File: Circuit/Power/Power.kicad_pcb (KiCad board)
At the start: 2 copper layers, 78.7 x 45.7 mm, 25 parts, among them J1 +-12V Pulse in, J2 To Starter & Coil, J3 To Capacitors, J4 From Control, J5 12V DC in, Q1 IRFP250NPBF, Q2 IRFP250NPBF, Q3 IRFP250NPBF, Q4 IRFP250NPBF, Q5 IRFP250NPBF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

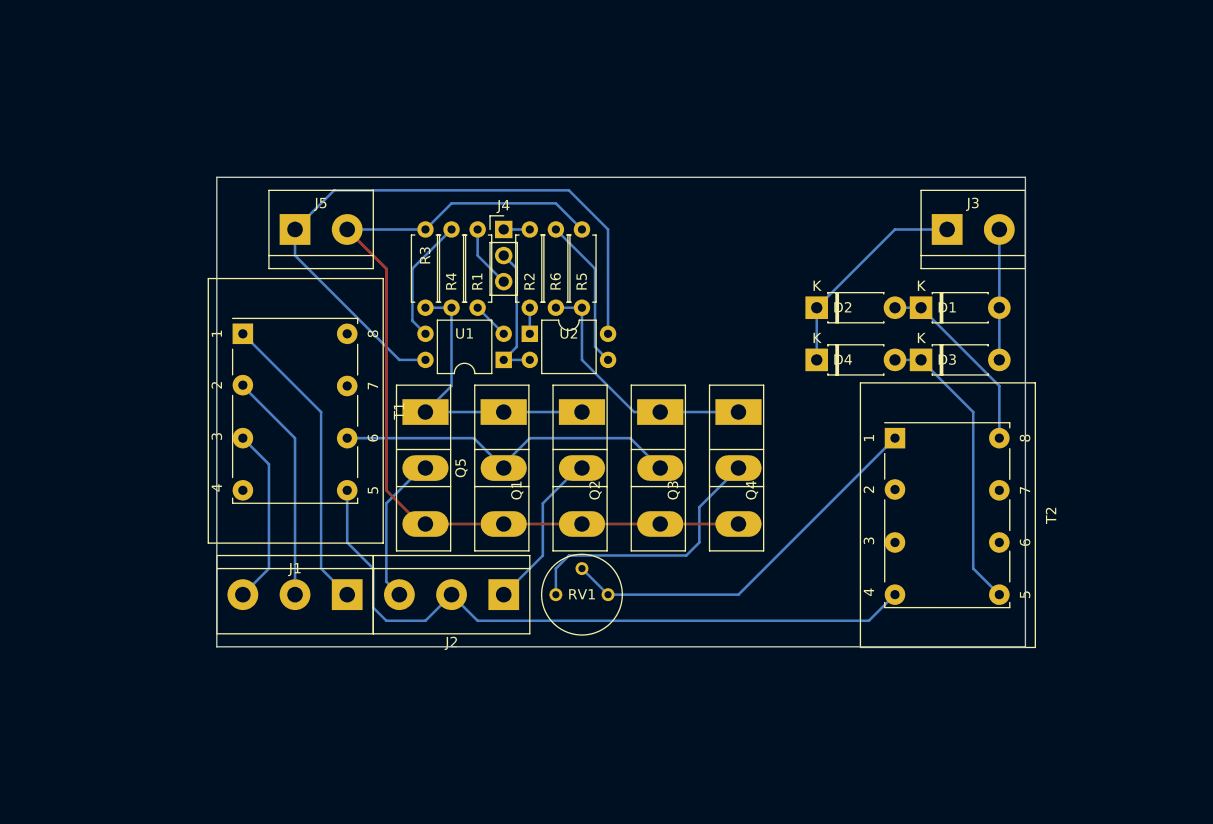
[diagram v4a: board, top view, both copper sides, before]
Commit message: [Circuit] Add a 1-stage Cockcroft–Walton generator to power module
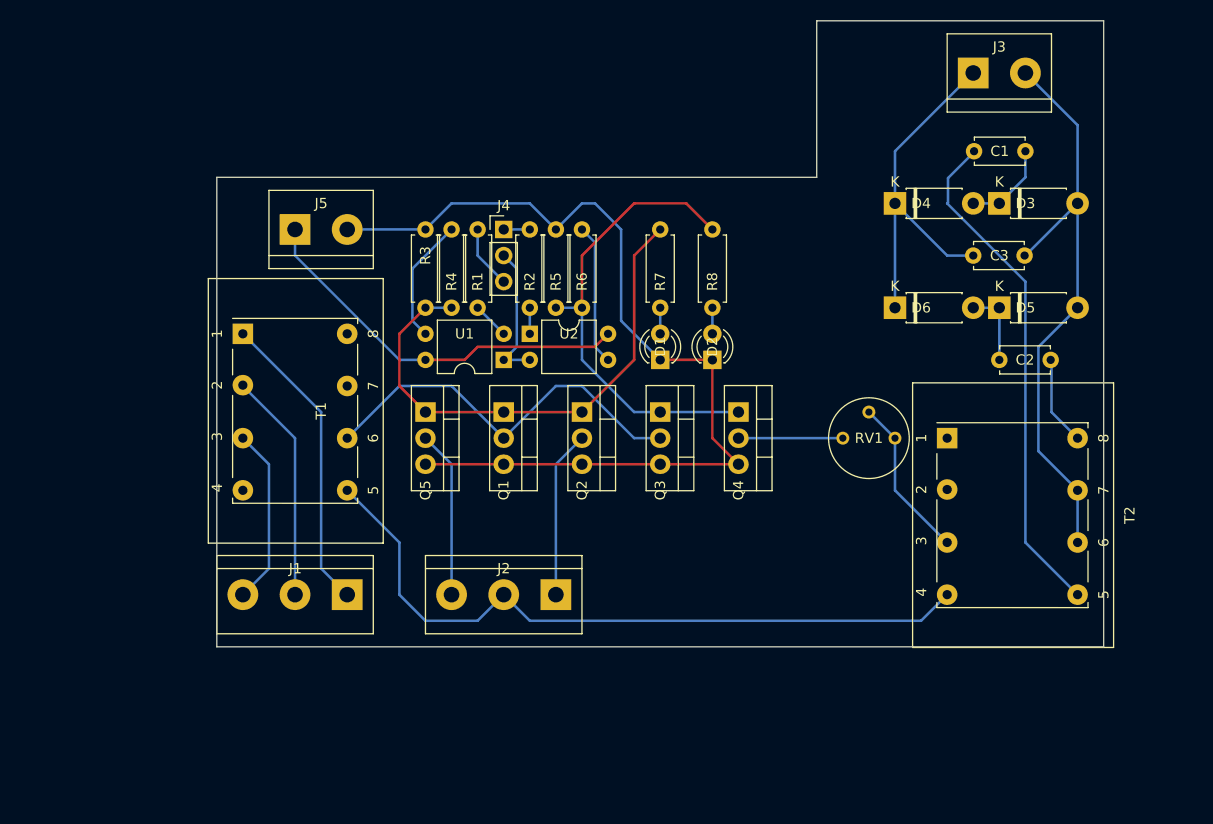
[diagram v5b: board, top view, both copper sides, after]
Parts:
- added C1: 1nF, Capacitor_THT:C_Disc_D4.7mm_W2.5mm_P5.00mm, F.Cu at (147.3, 33.0)
- added C2: 1nF, Capacitor_THT:C_Disc_D4.7mm_W2.5mm_P5.00mm, F.Cu at (144.8, 53.3)
- added C3: 1nF, Capacitor_THT:C_Disc_D4.7mm_W2.5mm_P5.00mm, F.Cu at (142.2, 43.2)
- added D1: LED, LED_THT:LED_D3.0mm_FlatTop, F.Cu at (111.8, 53.3)
- added D2: LED, LED_THT:LED_D3.0mm_FlatTop, F.Cu at (116.8, 53.3)
- added R7: 2K2, Resistor_THT:R_Axial_DIN0207_L6.3mm_D2.5mm_P7.62mm_Horizontal, F.Cu at (111.8, 48.3)
- added R8: 2K2, Resistor_THT:R_Axial_DIN0207_L6.3mm_D2.5mm_P7.62mm_Horizontal, F.Cu at (116.8, 40.6)
- J1: value +-12V Pulse in -> 12V AC in
- Q1, Q2, Q3, Q4, Q5: value IRFP250NPBF -> RFP30N06LE; footprint Package_TO_SOT_THT:TO-247-3_Vertical -> Package_TO_SOT_THT:TO-220-3_Vertical
- R4, R6: value 100 -> 10K
- T1: value 4+4:8 -> 3+3:6
- moved RV1 31.8 mm to (129.5, 61.0)
- moved J3 15.5 mm to (142.2, 25.4)
- moved D3 12.7 mm to (144.8, 38.1)
- moved D4 12.7 mm to (134.6, 38.1)
- moved D5 9.16 mm to (144.8, 48.3)
- moved D6 9.16 mm to (134.6, 48.3)
- moved J2 5.08 mm to (101.6, 76.2)
- moved T2 5.08 mm to (139.7, 61.0)
- moved R5 2.54 mm to (101.6, 48.3)
- moved R6 2.54 mm to (104.1, 40.6)
- renumbered D1 to D3, D2 to D4, D3 to D5, D4 to D6
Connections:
- net /+12VPulseIn renamed /AC+In
- net /-12VPulseIn renamed /AC-In
- net /0Vin renamed /AC0In
- D3 pad 1: Net-(D1-Pad1) -> Net-(C1-Pad1)
- D4 pad 2: Net-(D1-Pad1) -> Net-(C1-Pad1)
- D5 pad 1: Net-(D3-Pad1) -> Net-(C2-Pad1)
- D6 pad 2: Net-(D3-Pad1) -> Net-(C2-Pad1)
- T2 pad 1: Net-(RV1-Pad2) -> (no net)
- T2 pad 3: (no net) -> Net-(RV1-Pad2)
- T2 pad 5: Net-(D3-Pad1) -> Net-(C1-Pad2)
- T2 pad 6: (no net) -> /CapacitorPower-
- T2 pad 7: (no net) -> /CapacitorPower-
- T2 pad 8: Net-(D1-Pad1) -> Net-(C2-Pad2)
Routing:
- net Net-(C1-Pad2): track 0.00 -> 49.5 mm
- net /CapacitorPower-: track 12.7 -> 58.2 mm
- net Net-(D3-Pad1): track 28.6 -> 0.00 mm
- net +12V: track 63.2 -> 38.3 mm
- net Net-(Q1-Pad1): track 29.0 -> 51.0 mm
- net Net-(RV1-Pad2): track 37.8 -> 15.9 mm
- net Net-(Q3-Pad1): track 25.0 -> 45.9 mm
- net Net-(D1-Pad1): track 18.4 -> 0.00 mm
- net Net-(Q4-Pad2): track 26.4 -> 10.2 mm
- net /CapacitorPower+: track 20.9 -> 35.7 mm
- net Net-(C2-Pad2): track 0.00 -> 8.67 mm
- net Net-(C1-Pad1): track 0.00 -> 8.67 mm
- net Net-(C2-Pad1): track 0.00 -> 7.62 mm
- net GND: track 87.6 -> 93.0 mm
- net Net-(Q1-Pad2): track 34.3 -> 38.9 mm
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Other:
- board size 78.7 x 45.7 mm -> 86.4 x 61 mm

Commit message: [Circuit] Change the isolation transformer to a toroid one
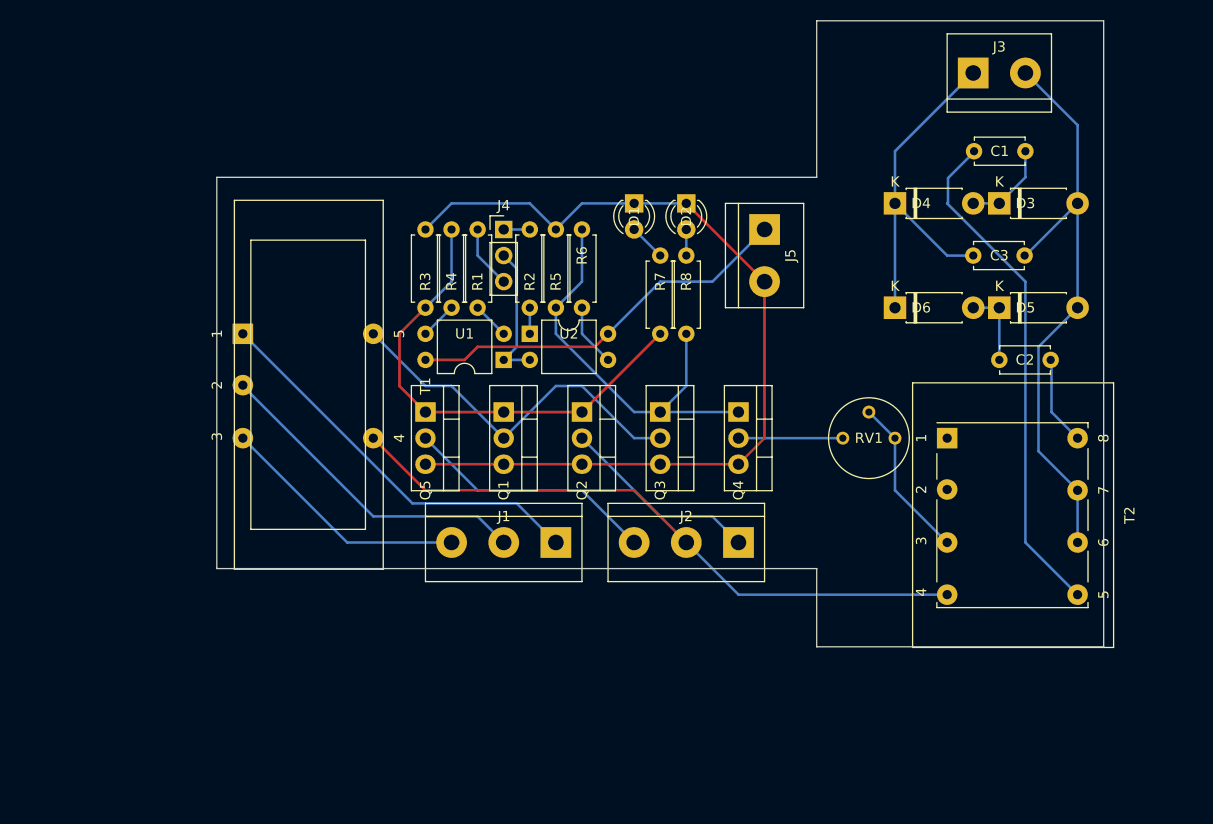
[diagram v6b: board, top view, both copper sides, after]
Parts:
- T1: footprint Power:Transformer_Generic_EE25_8Pin -> Power:Transformer_Toroid_5Pin
- moved J5 45.7 mm to (121.9, 40.6), turned to 270 degrees
- moved J1 20.9 mm to (101.6, 71.1)
- moved J2 18.5 mm to (119.4, 71.1)
- moved D1 15.5 mm to (109.2, 38.1), turned to 270 degrees
- moved D2 15.5 mm to (114.3, 38.1), turned to 270 degrees
- moved R8 10.5 mm to (114.3, 50.8), turned to 90 degrees
- moved R4 7.62 mm to (91.4, 48.3), turned to 90 degrees
- moved R6 7.62 mm to (104.1, 48.3), turned to 90 degrees
- moved T1 7.62 mm to (71.1, 43.2)
- moved R7 5.08 mm to (111.8, 43.2), turned to 270 degrees
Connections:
- T1 pad 4: (no net) -> /StarterPower-
- T1 pad 5: /StarterPower- -> Net-(Q1-Pad2)
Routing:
- net /AC0In: track 22.4 -> 31.8 mm
- net /AC+In: track 29.6 -> 38.9 mm
- net Net-(R4-Pad1): track 12.3 -> 3.59 mm
- net /CoilControl: track 16.3 -> 24.5 mm
- net Net-(R6-Pad1): track 13.8 -> 6.13 mm
- net /StarterPower-: track 69.8 -> 62.2 mm
- net /AC-In: track 17.4 -> 24.6 mm
- net Net-(Q3-Pad1): track 45.9 -> 40.8 mm
- net Net-(Q1-Pad1): track 51.0 -> 47.0 mm
- net GND: track 93.0 -> 89.8 mm
- net /StarterPower+: track 16.3 -> 19.4 mm
- net Net-(Q1-Pad2): track 38.9 -> 36.4 mm
- net Net-(D1-Pad2): track 2.54 -> 3.59 mm
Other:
- outline, holes or cut-outs redrawn

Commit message: [Circuit] Optimize the PCB of power module
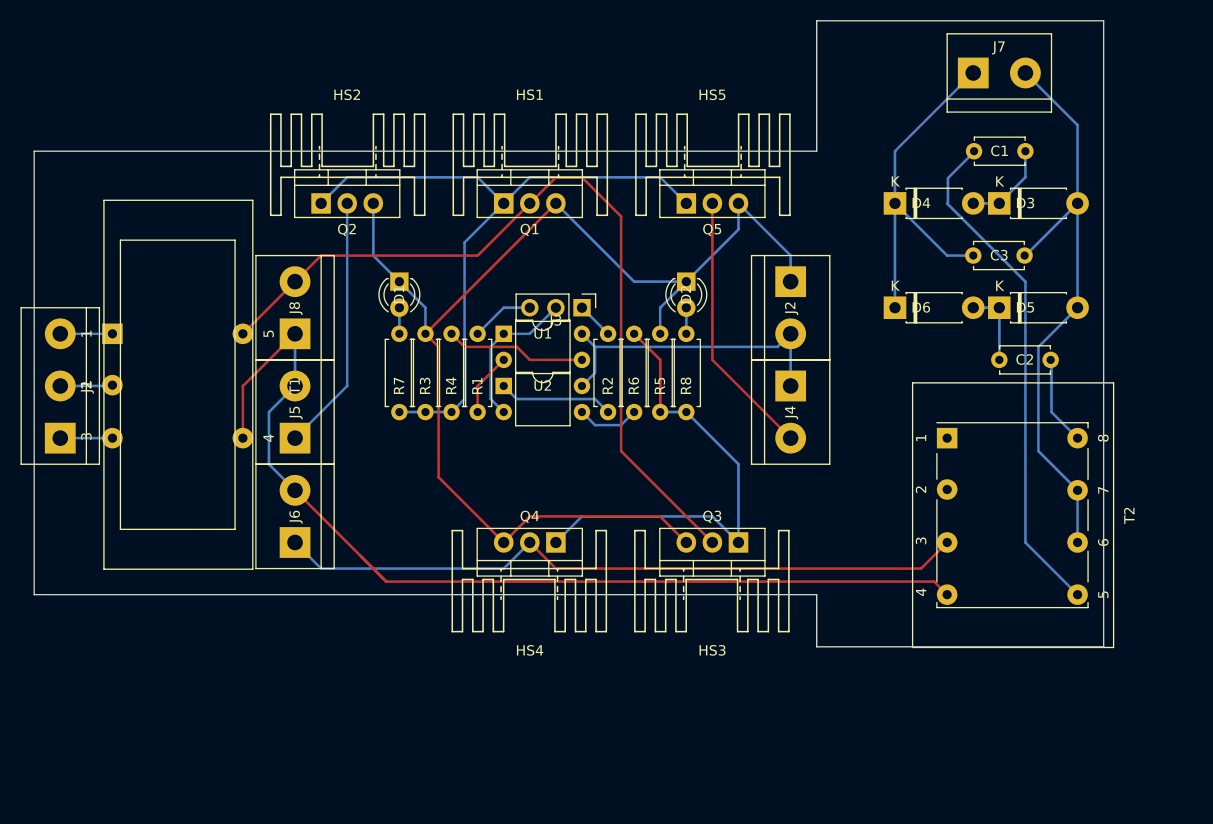
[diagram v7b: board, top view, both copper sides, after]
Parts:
- removed the J2 at (119.4, 71.1)
- removed RV1: 50K, Potentiometer_THT:Potentiometer_Bourns_3339P_Vertical
- added HS1: Heatsink, Power:Heatsink_TO220_15x10mm, F.Cu at (99.1, 35.6)
- added HS2: Heatsink, Power:Heatsink_TO220_15x10mm, F.Cu at (81.3, 35.6)
- added HS3: Heatsink, Power:Heatsink_TO220_15x10mm, F.Cu at (116.8, 73.7)
- added HS4: Heatsink, Power:Heatsink_TO220_15x10mm, F.Cu at (99.1, 73.7)
- added HS5: Heatsink, Power:Heatsink_TO220_15x10mm, F.Cu at (116.8, 35.6)
- added J4: To Coil, TerminalBlock:TerminalBlock_bornier-2_P5.08mm, F.Cu at (124.5, 55.9)
- added J5: To Starter, TerminalBlock:TerminalBlock_bornier-2_P5.08mm, F.Cu at (76.2, 61.0)
- added J6: To Capacitor, TerminalBlock:TerminalBlock_bornier-2_P5.08mm, F.Cu at (76.2, 71.1)
- added J8: AC In, TerminalBlock:TerminalBlock_bornier-2_P5.08mm, F.Cu at (76.2, 50.8)
- D1: value LED -> Discharge
- D2: value LED -> Charge
- J1: value 12V AC in -> 12V AC In
- J2: renamed from J5; value 12V DC in -> DC In
- R7, R8: value 2K2 -> 3K3
- T1: value 3+3:6 -> 7+7:14
- moved J1 49.3 mm to (53.3, 61.0), turned to 90 degrees
- moved Q2 32.5 mm to (78.7, 38.1), turned to 0 degrees
- moved Q5 32.5 mm to (114.3, 38.1), turned to 0 degrees
- moved R7 26.5 mm to (86.4, 50.8)
- moved D1 24.1 mm to (86.4, 45.7)
- moved Q4 21.8 mm to (101.6, 71.1), turned to 180 degrees
- moved Q1 20.3 mm to (96.5, 38.1), turned to 0 degrees
- moved Q3 14.8 mm to (119.4, 71.1), turned to 180 degrees
- moved R5 14.4 mm to (111.8, 58.4)
- moved T1 12.7 mm to (58.4, 43.2)
- moved R2 12.7 mm to (106.7, 50.8)
- moved R6 11.4 mm to (109.2, 58.4)
- moved J3 10.8 mm to (104.1, 48.3), turned to 270 degrees
- moved R1 10.2 mm to (94.0, 50.8)
- moved R3 10.2 mm to (88.9, 50.8)
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- renumbered J4 to J3, J3 to J7
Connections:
- J1 pad 1: /AC+In -> /AC-In
- J1 pad 3: /AC-In -> /AC+In
- J2 pad 1: +12V -> GND
- J2 pad 2: GND -> +12V
- Q4 pad 2: Net-(Q4-Pad2) -> Net-(J6-Pad1)
- Q5 pad 2: /CoilControl -> /Coil-
- T2 pad 3: Net-(RV1-Pad2) -> Net-(J6-Pad1)
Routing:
- net Net-(J6-Pad1): track 0.00 -> 67.7 mm
- net Net-(J8-Pad2): track 36.4 -> 80.2 mm
- net /StarterPower-: track 62.2 -> 100.9 mm
- net /AC+In: track 38.9 -> 5.08 mm
- net GND: track 89.8 -> 117.6 mm
- net /AC0In: track 31.8 -> 5.11 mm
- net /Coil-: track 0.00 -> 26.0 mm
- net /CoilControl: track 24.5 -> 0.00 mm
- net Net-(Q1-Pad1): track 47.0 -> 67.3 mm
- net /AC-In: track 24.6 -> 5.08 mm
- net Net-(RV1-Pad2): track 15.9 -> 0.00 mm
- net Net-(R4-Pad1): track 3.59 -> 13.8 mm
- net Net-(Q4-Pad2): track 10.2 -> 0.00 mm
- net Net-(R2-Pad2): track 2.54 -> 11.2 mm
- net +12V: track 38.3 -> 30.8 mm
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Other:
- board size 86.4 x 61 mm -> 104.1 x 61 mm
